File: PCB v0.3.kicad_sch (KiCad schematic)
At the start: 67 parts, among them J1 XT60-M, J10 Screw 2.54mm 5P, J11 Screw 2.54mm 5P, J12 Screw 2.54mm 5P, J13 2.54mm 3P, J14 2.54mm 3P, J15 2.54mm 3P, J16 2.54mm 3P, J17 JST-SH 3P, J18 JST-SH 3P, J19 JST-SH 3P, J2 Raspberry Pi 5, J20 JST-SH 3P, J21 JST-SH 3P, J22 JST-SH 3P, J3 XT30-F, J4 XT30-M, J5 XT30-F, J6 XT30-M, J7 Screw 2.54mm 5P, J8 Screw 2.54mm 5P, J9 Screw 2.54mm 5P, Q1 NCE15P25JK, U1 3.2~32V -> 5.1V 5A

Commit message: Changed PCB
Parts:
- added R9: 470R 0805, Resistor_SMD:R_0805_2012Metric_Pad1.20x1.40mm_HandSolder, symbol Device:R
- F1: value 30A -> 15A
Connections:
- net at D6.1 (K): now also R9.2; no longer R6.2
- new net: R6.2, R9.1
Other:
- note added: "Adjustable XL4015 buck converter module. Change until Raspberry Pi 5V pin is exactly 5.1V"
- note added: "External DC/DC Converter Recommended >10 A"
- note added: "External DC/DC Converter Recommended >10.8 A"
- note added: "Recommended 36GP-3626 43RPM 12V w/ built-in PWM speed controller"
- note added: "Recommended ST3215-7.4V Servo"
- note removed: "Adjustable buck converter. Change until Raspberry Pi 5V pin is exactly 5.1V"
- note removed: "External DC/DC Converter"
- company: HKU ROVER Team -> HKU Martians
- title: Prototype Rover PCB v0.1 -> Prototype Rover PCB v0.3

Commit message: Finished v0.3 SCH
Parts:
- removed C1: 1000u 50V (E), Capacitor_THT:CP_Radial_D13.0mm_P5.00mm, symbol Device:C_Polarized
- removed C10, C11, C8, C9: 100u 50V (E), Capacitor_THT:CP_Radial_D8.0mm_P3.50mm, symbol Device:C_Polarized
- removed C7: 0.1u 50V 1206 (C), Capacitor_SMD:C_1206_3216Metric_Pad1.33x1.80mm_HandSolder, symbol Device:C
- removed D2: 3.3V, Diode_SMD:Nexperia_CFP3_SOD-123W, symbol Device:D_Zener
- removed F3: 500mA 1206, Fuse:Fuse_1206_3216Metric, symbol Device:Polyfuse
- removed FB1, FB2, FB3: BLM21PG220, Inductor_SMD:L_0805_2012Metric_Pad1.05x1.20mm_HandSolder, symbol Device:FerriteBead
- added C2, C3: 0.1u 50V 1206 (C), Capacitor_SMD:C_1206_3216Metric_Pad1.33x1.80mm_HandSolder, symbol Device:C
- added C5: 470u 50V (E), Capacitor_THT:CP_Radial_D10.0mm_P5.00mm, symbol Device:C_Polarized
- added C6: 1000u 50V (E), Capacitor_THT:CP_Radial_D13.0mm_P5.00mm, symbol Device:C_Polarized
- C4: renamed from C3; value 0.1u 50V 1206 (C) -> 100n 50V 1206 (C)
- J11: renamed from J7; value Screw 2.54mm 5P -> 2.54mm 5P Terminal Block
- J12: renamed from J8; value Screw 2.54mm 5P -> 2.54mm 5P Terminal Block
- J13: renamed from J9; value Screw 2.54mm 5P -> 2.54mm 5P Terminal Block
- J14: renamed from J10; value Screw 2.54mm 5P -> 2.54mm 5P Terminal Block
- J15: renamed from J11; value Screw 2.54mm 5P -> 2.54mm 5P Terminal Block
- J16: renamed from J12; value Screw 2.54mm 5P -> 2.54mm 5P Terminal Block
- Q1: Taobao https://item.taobao.com/item.htm?id=809752933171&spm=a312a.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 -> https://item.taobao.com/item.htm?from=cart&id=810052647977&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
- renumbered C2 to C1, C5 to C7, C6 to C8, C4 to C9, D3 to D2, D4 to D3, D5 to D4, D6 to D5, D7 to D6, D8 to D7, J16 to J10, J13 to J7, J14 to J8, J15 to J9, R9 to R5, R5 to R6, R6 to R7, R7 to R8, R8 to R9, TP6 to TP5, TP5 to TP6
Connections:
- net +12V: now also C6.1
- net +3V3: now also A1.35 (ADC_VREF), C4.1
- net +5.1V: now also A1.39 (VSYS), J2.2 (5V), J2.4 (5V), C2.1, C3.1; no longer U1.1 (+VDC)
- net +7.5V: now also C5.1
- net GND: now also C2.2, C3.2, C5.2, C6.2
- net at F2.1: now also U1.1 (+VDC)
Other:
- note removed: "Warning: No back-power protection. Use an isolator if connecting directly to Pi with USB. Remote PC preferred."
- moved on the sheet: C1, C7, C8, C9, D2, D3, J10, J11, J12, J13, J14, J15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

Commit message: Laid out power circuitry
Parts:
- F1: footprint Fuse:FuseHolder_Blade_ATO_Littelfuse_FLR_178.6165 -> Fuse:Fuse_Blade_ATO_directSolder
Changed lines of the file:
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@@
 			)
 		)
-		(property "Footprint" "Fuse:FuseHolder_Blade_ATO_Littelfuse_FLR_178.6165"
+		(property "Footprint" "Fuse:Fuse_Blade_ATO_directSolder"
 			(at 63.5 38.608 90)
 			(hide yes)

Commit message: Finished laying out
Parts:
- F2: footprint Fuse:Fuse_1206_3216Metric -> Fuse:Fuse_1812_4532Metric_Pad1.30x3.40mm_HandSolder
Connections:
- net GND: now also A1.33 (AGND)
- no-connect marks 34 -> 33
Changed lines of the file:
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@@
 	)
 	(no_connect
-		(at 365.76 102.87)
-	)
-	(no_connect
 		(at 246.38 71.12)
 	)
@@
 	(wire
 		(pts
+			(xy 368.3 104.14) (xy 368.3 102.87)
+		)
+		(stroke
+			(width 0)
+			(type default)
+		)
+	)
+	(wire
+		(pts
 			(xy 80.01 44.45) (xy 87.63 44.45)
 		)
@@
 	(wire
 		(pts
+			(xy 368.3 102.87) (xy 365.76 102.87)
+		)
+		(stroke
+			(width 0)
+			(type default)
+		)
+	)
+	(wire
+		(pts
 			(xy 308.61 74.93) (xy 320.04 74.93)
 		)
@@
 	)
 	(symbol
+		(lib_id "power:GND")
+		(at 368.3 104.14 0)
+		(unit 1)
+		(body_style 1)
+		(exclude_from_sim no)
+		(in_bom yes)
+		(on_board yes)
+		(in_pos_files yes)
+		(dnp no)
+		(fields_autoplaced yes)
+		(property "Reference" "#PWR078"
+			(at 368.3 110.49 0)
+			(hide yes)
+			(show_name no)
+			(do_not_autoplace no)
+			(effects
+				(font
+					(size 1.27 1.27)
+				)
+			)
+		)
+		(property "Value" "GND"
+			(at 368.3 109.22 0)
+			(hide yes)
+			(show_name no)
+			(do_not_autoplace no)
+			(effects
+				(font
+					(size 1.27 1.27)
+				)
+			)
+		)
+		(property "Footprint" ""
+			(at 368.3 104.14 0)
+			(hide yes)
+			(show_name no)
+			(do_not_autoplace no)
+			(effects
+				(font
+					(size 1.27 1.27)
+				)
+			)
+		)
+		(property "Datasheet" ""
+			(at 368.3 104.14 0)
+			(hide yes)
+			(show_name no)
+			(do_not_autoplace no)
+			(effects
+				(font
+					(size 1.27 1.27)
+				)
+			)
+		)
+		(property "Description" "Power symbol creates a global label with name \"GND\" , ground"
+			(at 368.3 104.14 0)
+			(hide yes)
+			(show_name no)
+			(do_not_autoplace no)
+			(effects
+				(font
+					(size 1.27 1.27)
+				)
+			)
+		)
+		(pin "1"
+		)
+		(instances
+			(project "PCB v0.3"
+				(path "/4a9ac192-968f-45b6-b822-e3973cb892fb"
+					(reference "#PWR078")
+					(unit 1)
+				)
+			)
+		)
+	)
+	(symbol
 		(lib_id "Connector:TestPoint")
 		(at 62.23 111.76 270)
@@
 			)
 		)
-		(property "Footprint" "Fuse:Fuse_1206_3216Metric"
+		(property "Footprint" "Fuse:Fuse_1812_4532Metric_Pad1.30x3.40mm_HandSolder"
 			(at 95.25 185.42 0)
 			(hide yes)

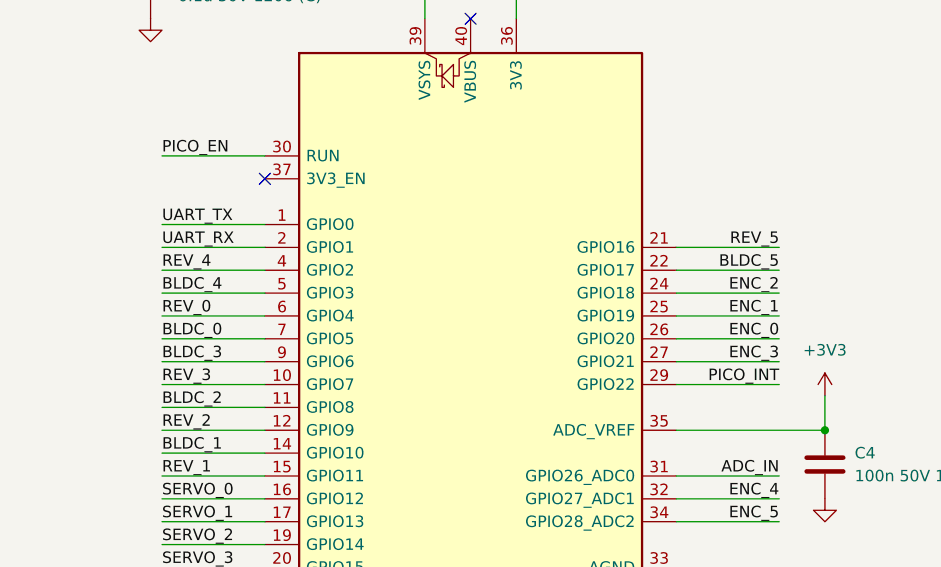
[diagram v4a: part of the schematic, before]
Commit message: Power planes, began routing
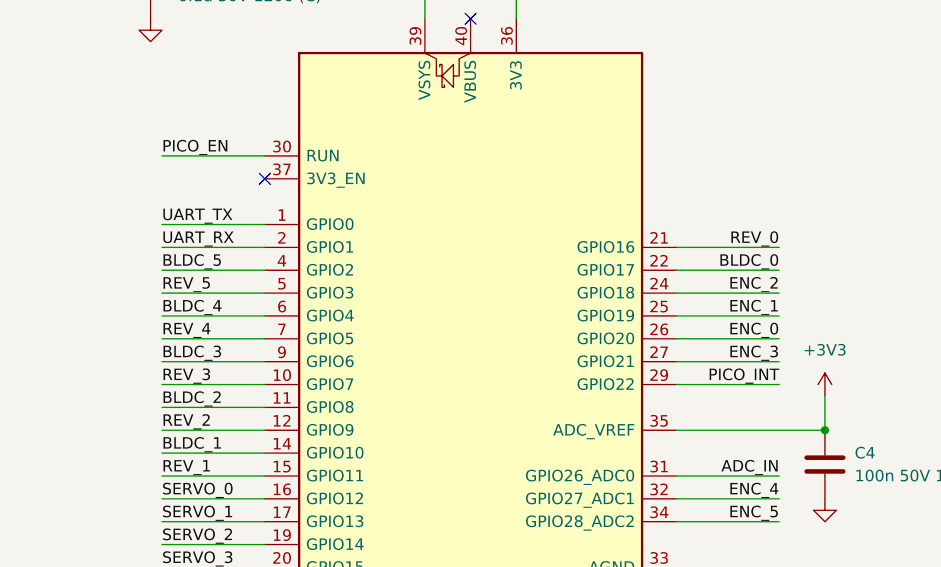
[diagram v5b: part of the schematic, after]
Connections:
- net BLDC_0: now also A1.22 (GPIO17); no longer A1.7 (GPIO5)
- net BLDC_4: now also A1.6 (GPIO4); no longer A1.5 (GPIO3)
- net BLDC_5: now also A1.4 (GPIO2); no longer A1.22 (GPIO17)
- net REV_0: now also A1.21 (GPIO16); no longer A1.6 (GPIO4)
- net REV_4: now also A1.7 (GPIO5); no longer A1.4 (GPIO2)
- net REV_5: now also A1.5 (GPIO3); no longer A1.21 (GPIO16)

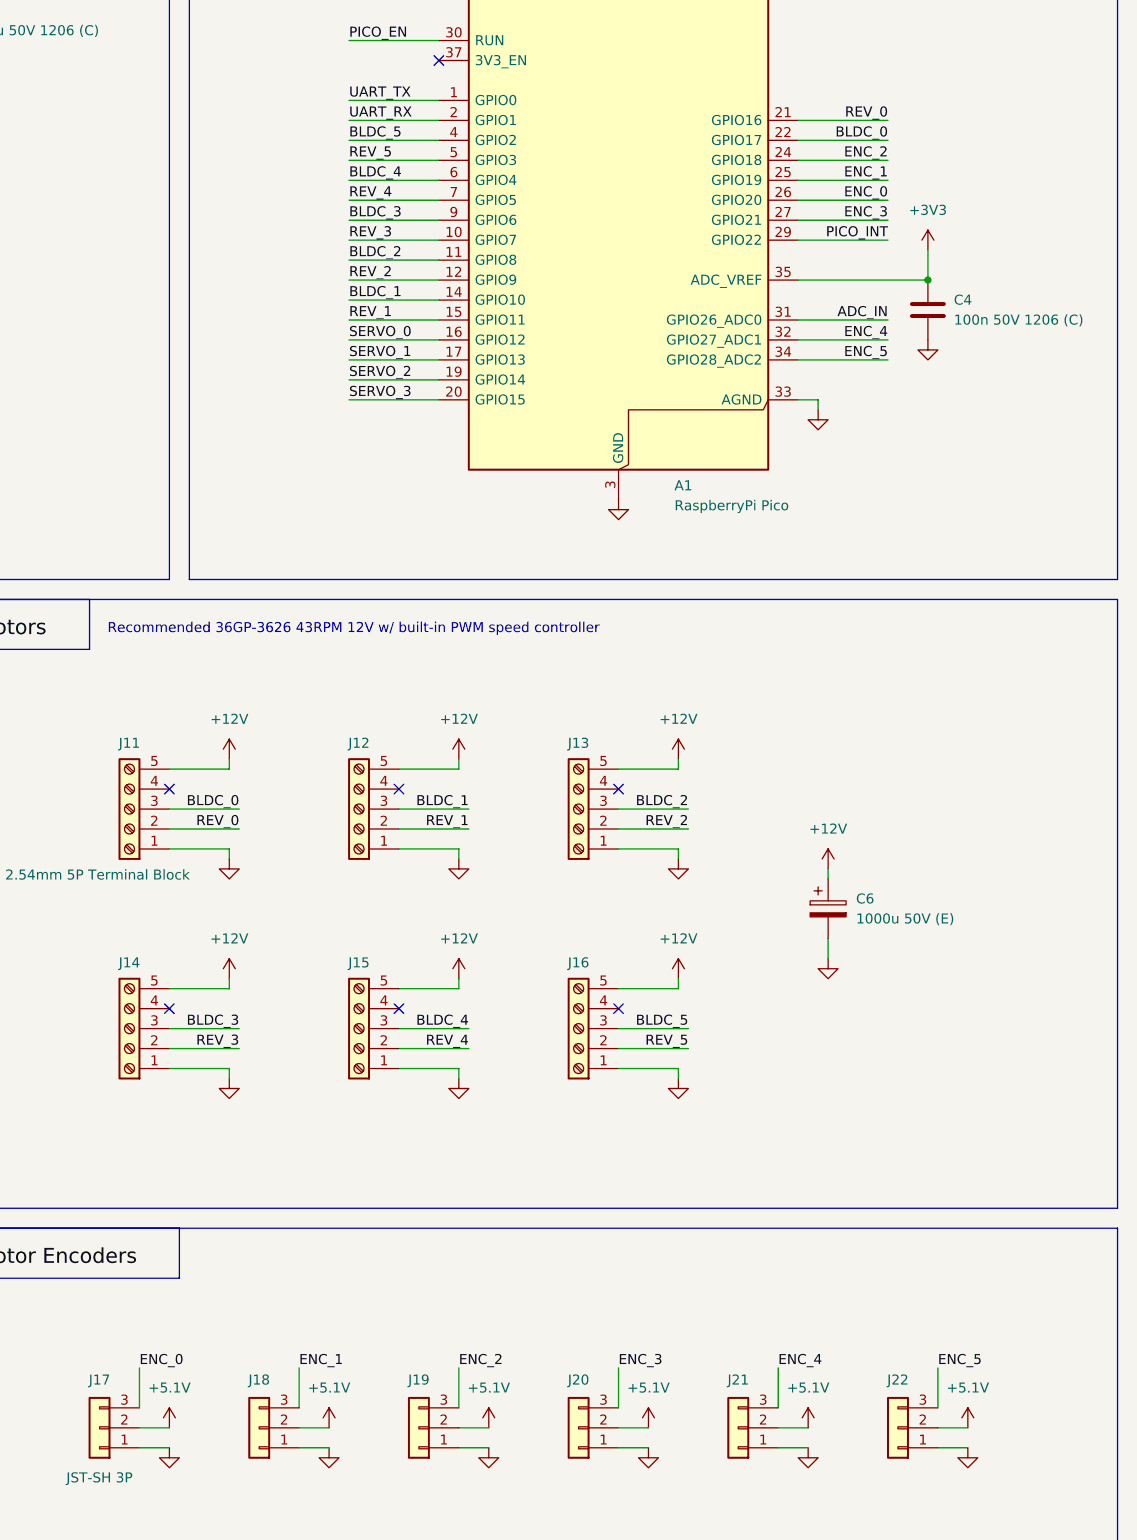
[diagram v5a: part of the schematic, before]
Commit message: Finished layout and routing. Begun documentation
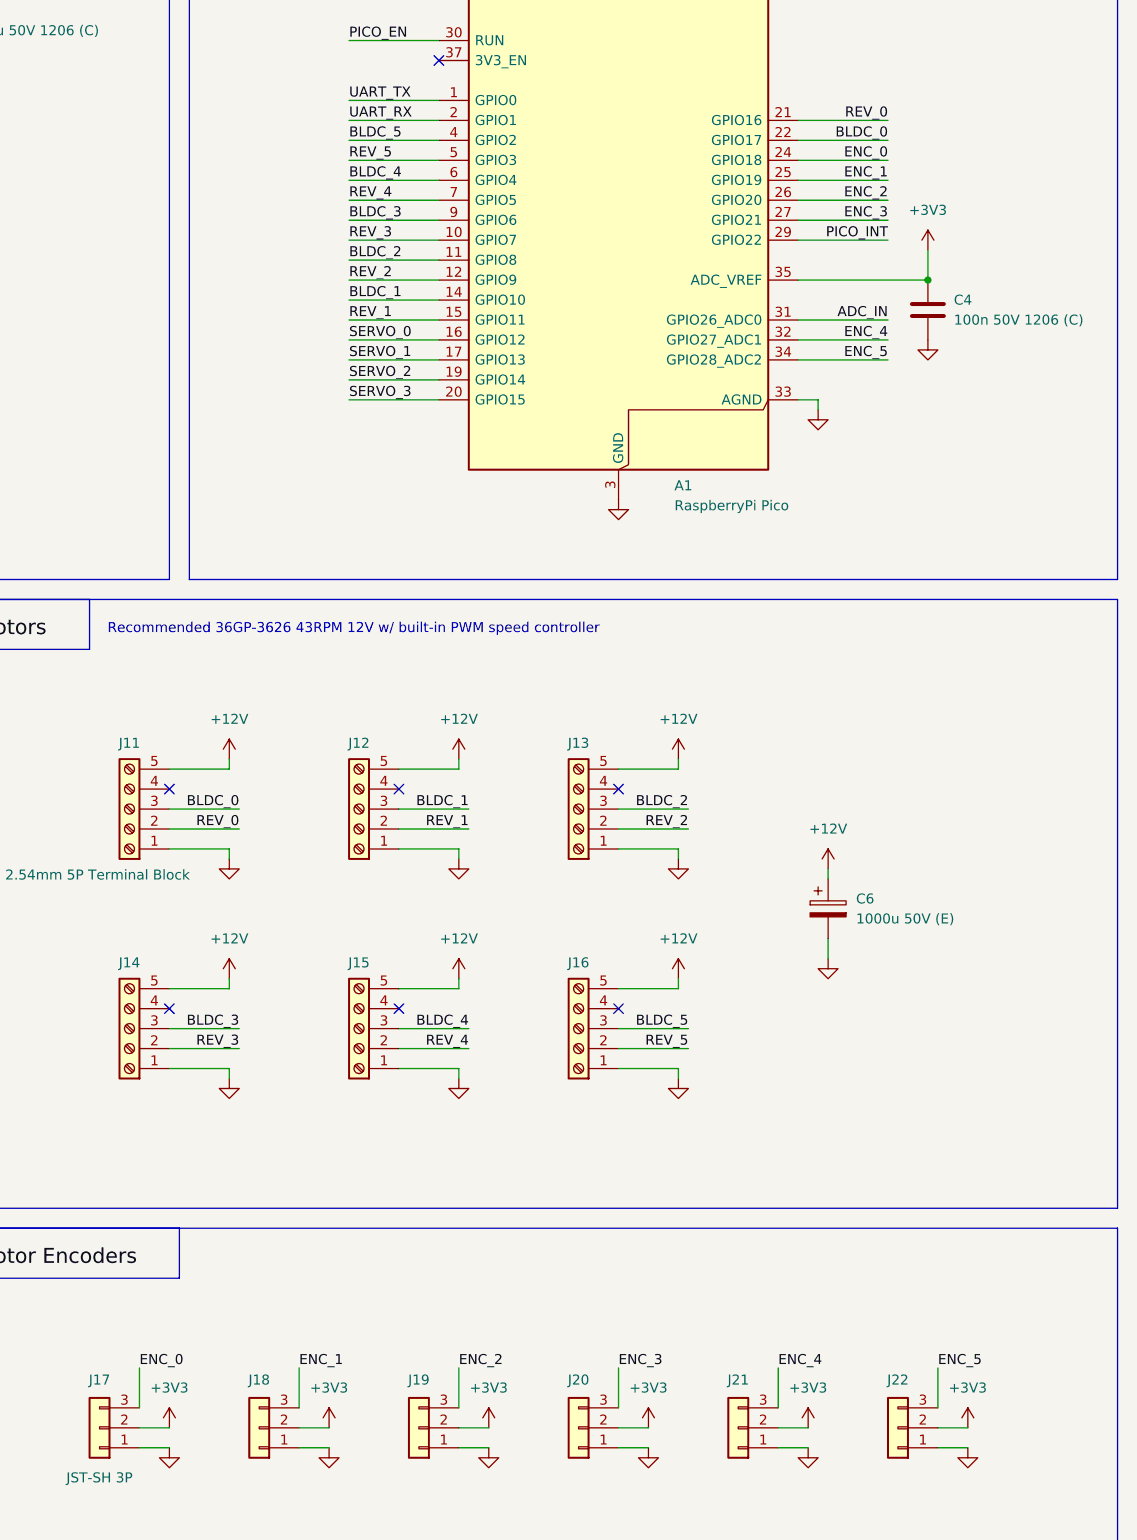
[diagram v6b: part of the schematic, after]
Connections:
- net +3V3: now also J17.2 (Pin_2), J18.2 (Pin_2), J19.2 (Pin_2), J20.2 (Pin_2), J21.2 (Pin_2), J22.2 (Pin_2)
- net +5.1V: no longer J17.2 (Pin_2), J18.2 (Pin_2), J19.2 (Pin_2), J20.2 (Pin_2), J21.2 (Pin_2), J22.2 (Pin_2)
- net ENC_0: now also A1.24 (GPIO18); no longer A1.26 (GPIO20)
- net ENC_2: now also A1.26 (GPIO20); no longer A1.24 (GPIO18)
